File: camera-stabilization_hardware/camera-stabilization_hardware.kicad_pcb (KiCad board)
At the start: 2 copper layers, 34.2 x 3.2 mm, 17 parts, among them J1 Conn_01x05_Pin, J2 Conn_01x05_Pin, J3 AVR-ISP-6, U1 ULN2003, U2 ULN2003, U3 ATmega328PB-A, Y1 Crystal_GND24

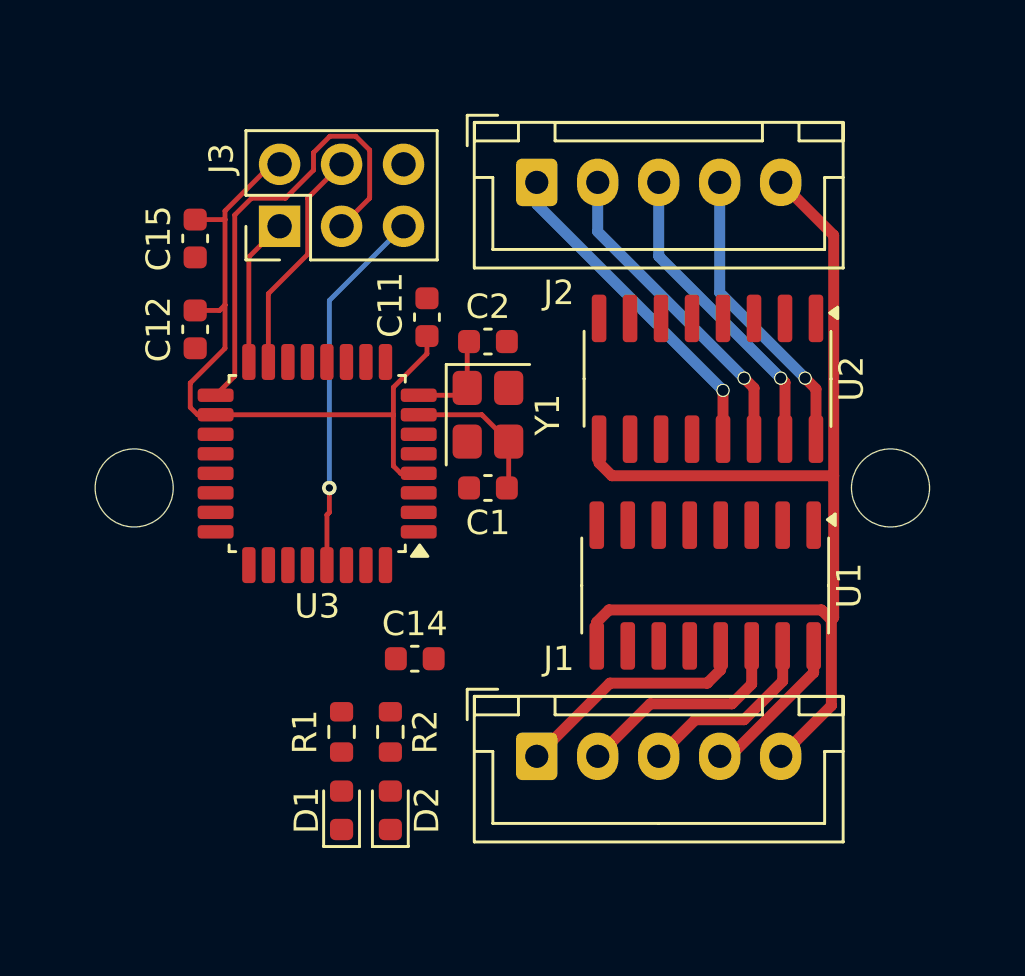
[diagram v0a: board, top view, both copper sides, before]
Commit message: added pcb wiring camera stabilization
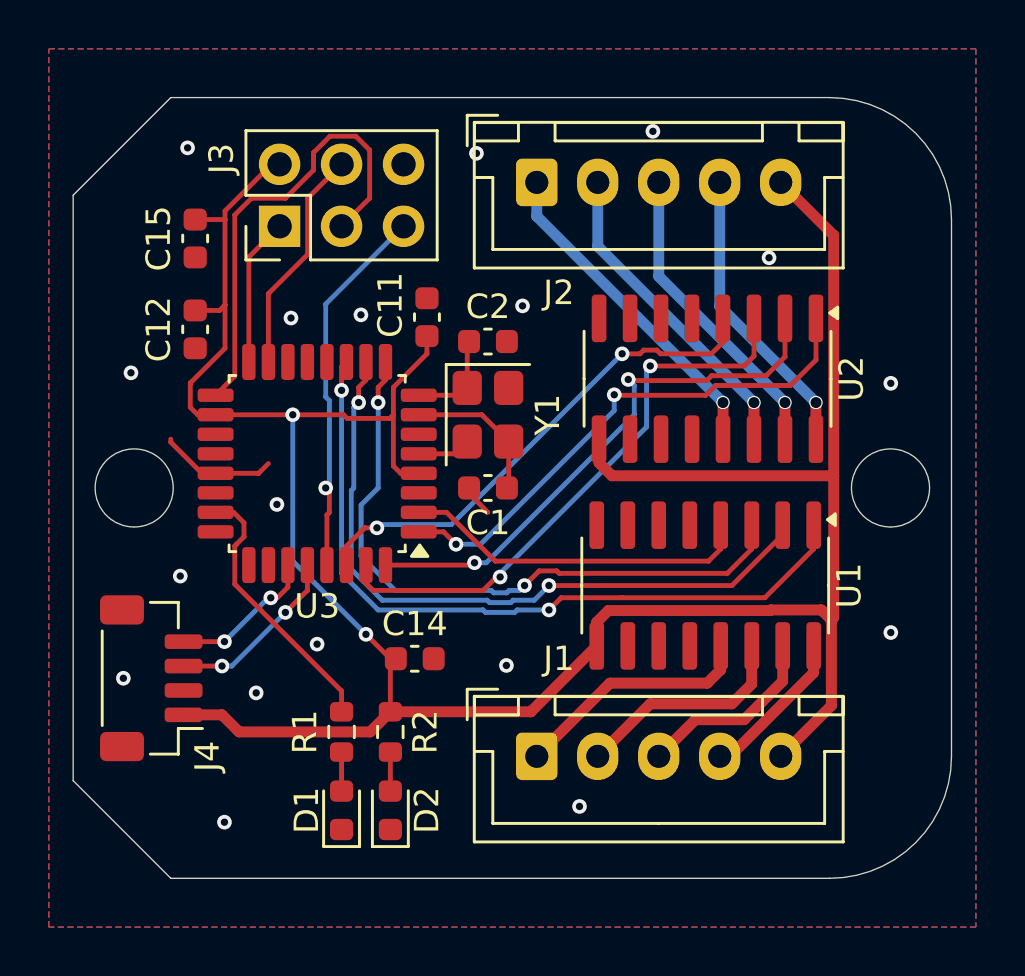
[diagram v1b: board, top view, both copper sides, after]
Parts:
- added J4: Conn_01x04_Pin, Connector_JST:JST_SH_BM04B-SRSS-TB_1x04-1MP_P1.00mm_Vertical, F.Cu at (107.2, 56.8)
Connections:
- C11 pad 1: VBUS -> +5V
- C12 pad 1: VBUS -> +5V
- C14 pad 1: VBUS -> +5V
- C15 pad 1: VBUS -> +5V
- J3 pad 2: VBUS -> +5V
- R2 pad 1: VBUS -> +5V
- U3 pad 1: unconnected-(U3-PD3-Pad1) -> INT5
- U3 pad 10: unconnected-(U3-PD6-Pad10) -> INT2
- U3 pad 11: unconnected-(U3-PD7-Pad11) -> INT1
- U3 pad 18: VBUS -> +5V
- U3 pad 2: unconnected-(U3-PD4-Pad2) -> INT4
- U3 pad 27: unconnected-(U3-PC4-Pad27) -> SDA
- U3 pad 28: unconnected-(U3-PC5-Pad28) -> SCL
- U3 pad 30: STEP -> INT8
- U3 pad 31: DIR -> INT7
- U3 pad 32: unconnected-(U3-PD2-Pad32) -> INT6
- U3 pad 4: VBUS -> +5V
- U3 pad 9: unconnected-(U3-PD5-Pad9) -> INT3
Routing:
- net +5V: track 47.1 -> 110.5 mm, vias 0 -> 2
- net INT1: track 0.00 -> 30.8 mm, vias 0 -> 2
- net VBUS: track 30.4 -> 0.00 mm
- net INT2: track 0.00 -> 28.5 mm, vias 0 -> 2
- net INT3: track 0.00 -> 26.8 mm, vias 0 -> 2
- net INT7: track 0.00 -> 23.8 mm, vias 0 -> 2
- net INT6: track 0.00 -> 22.7 mm, vias 0 -> 2
- net INT5: track 0.00 -> 21.7 mm, vias 0 -> 2
- net INT8: track 0.00 -> 20.8 mm, vias 0 -> 2
- net INT4: track 0.00 -> 14.4 mm
- net LED1: track 0.00 -> 11.1 mm
- net GND: track 0.00 -> 8.33 mm, vias 0 -> 18
- net SCL: track 0.00 -> 7.40 mm, vias 0 -> 2
- net SDA: track 0.00 -> 6.10 mm, vias 0 -> 2
- net Net-(D2-A): track 0.00 -> 1.60 mm
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- added copper zone on B.Cu, net GND
- added copper zone on F.Cu, net GND
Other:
- board size 34.2 x 3.2 mm -> 36 x 32 mm
